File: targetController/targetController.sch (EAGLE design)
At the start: 52 parts, among them Q1 MOSFET-NCHANNELBSS123LT1G, Q10 2n3904, Q11 MOSFET-NCHANNELBSS123LT1G, Q12 2n3904, Q13 MOSFET-NCHANNELBSS123LT1G, Q14 2n3904, Q15 MOSFET-NCHANNELBSS123LT1G, Q16 2n3904, Q17 MOSFET-NCHANNELBSS123LT1G, Q18 2n3904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

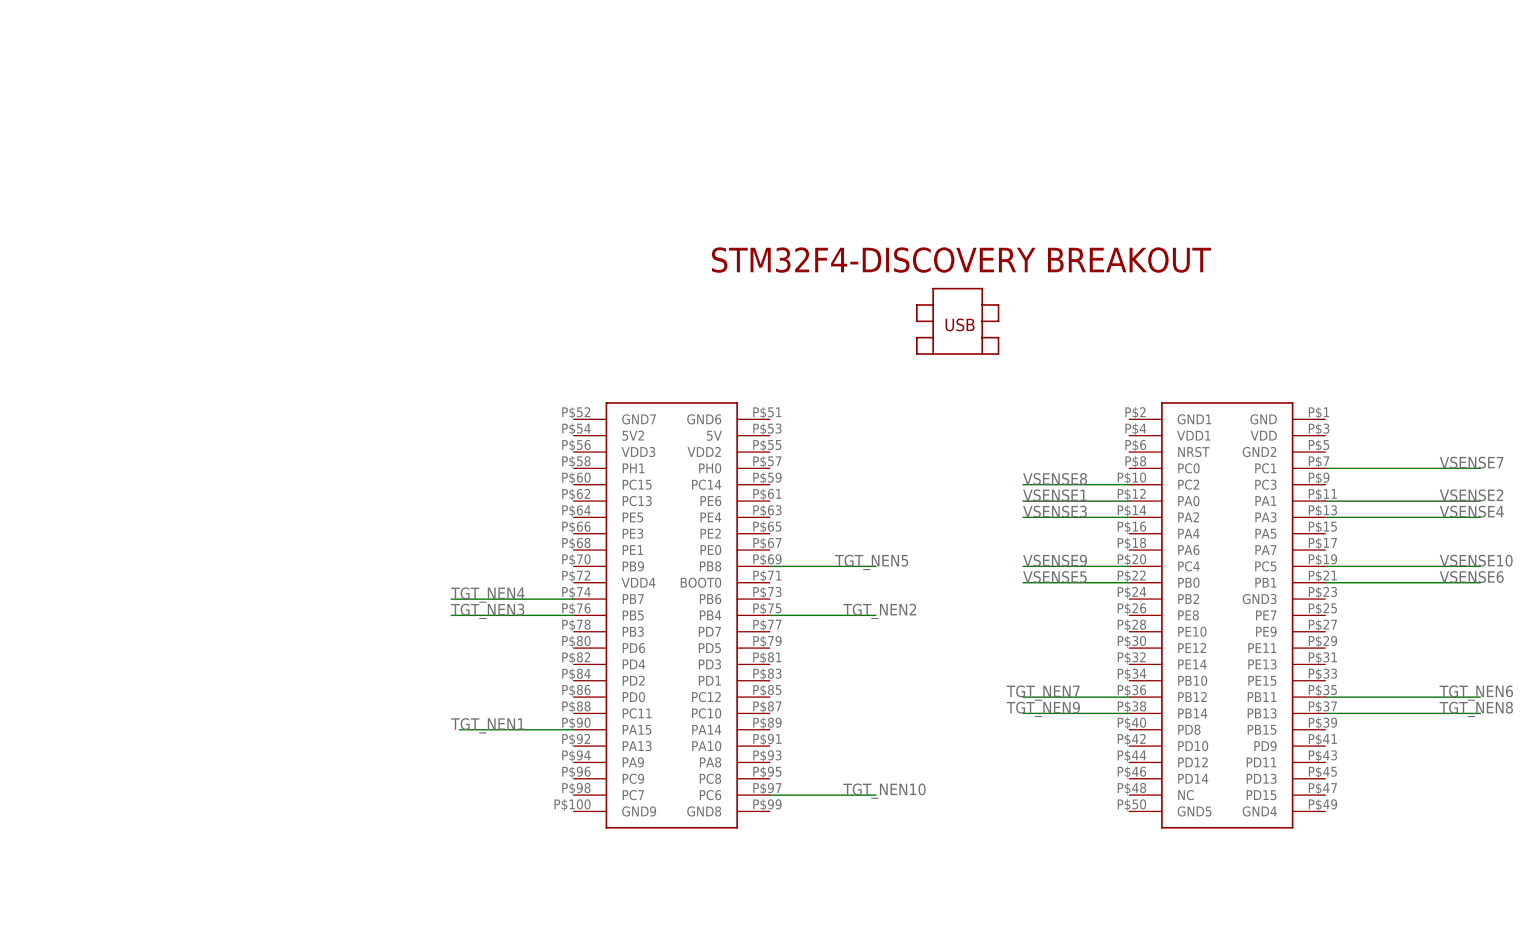
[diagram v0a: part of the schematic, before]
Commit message: Routed targetController
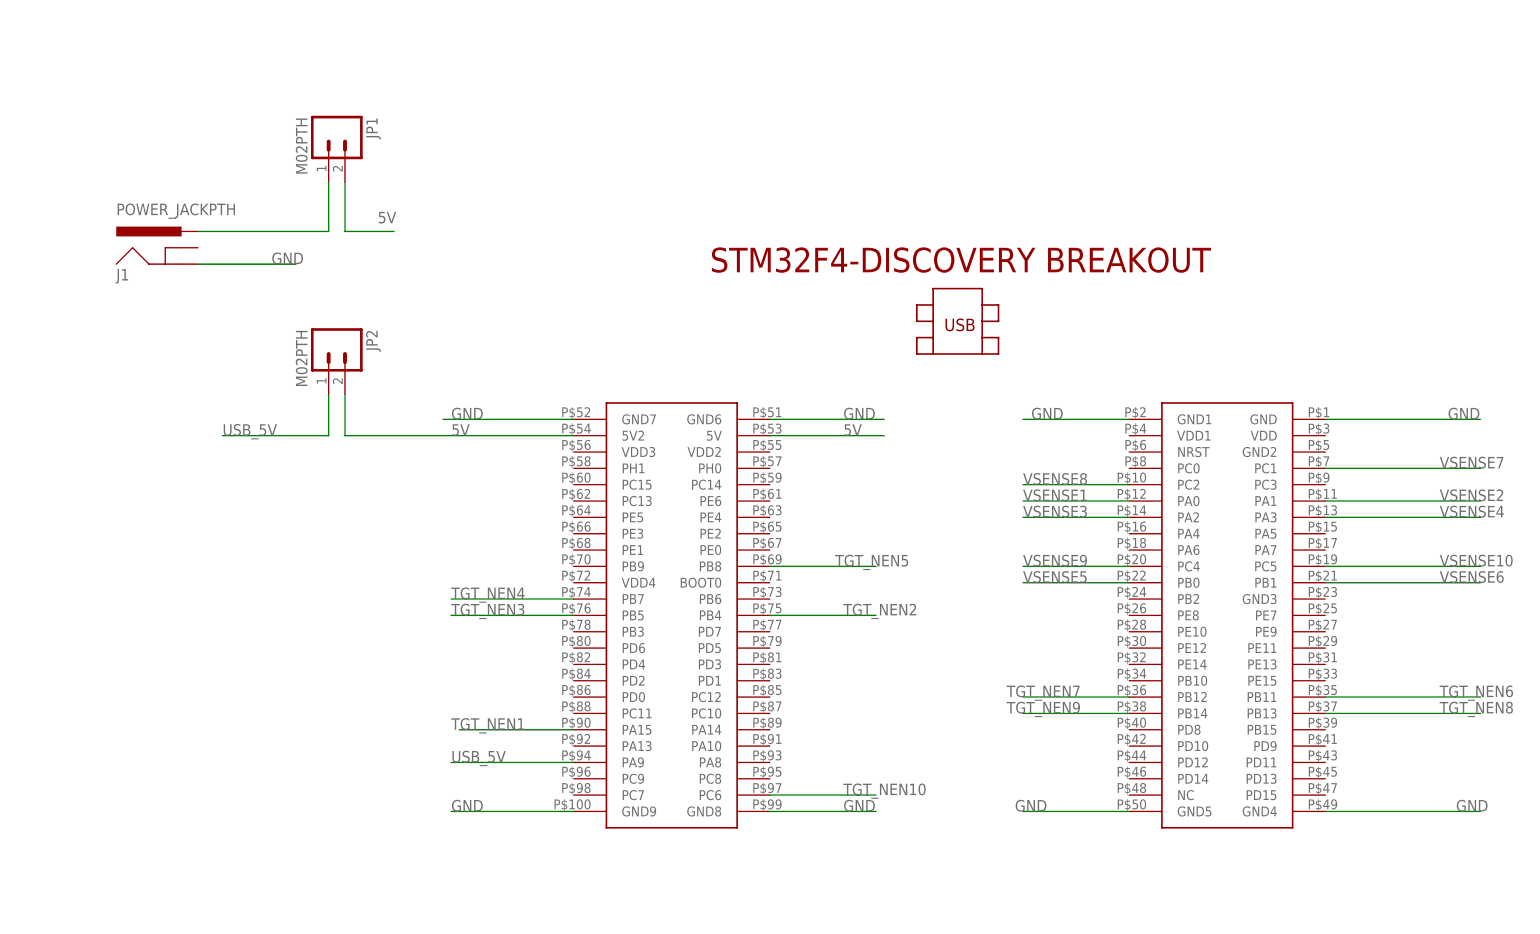
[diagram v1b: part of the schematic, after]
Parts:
- added J1: POWER_JACKPTH, SparkFun-Connectors:POWER_JACKPTH
- added JP1, JP2: M02PTH, SparkFun-Connectors:M02PTH
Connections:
- new net N$2: J1.PWR, JP1.1
- new net USB_5V: JP2.1, U$1.PA9
- net 5V: now also JP1.2, JP2.2, U$1.5V, U$1.5V2
- net GND: now also J1.GND, U$1.GND, U$1.GND1, U$1.GND4, U$1.GND5, U$1.GND6, U$1.GND7, U$1.GND8, U$1.GND9
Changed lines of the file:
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@@
 <setting verticaltext="up"/>
 </settings>
-<grid distance="0.1" unitdist="inch" unit="inch" style="lines" multiple="1" display="no" altdistance="0.01" altunitdist="inch" altunit="inch"/>
+<grid distance="0.05" unitdist="inch" unit="inch" style="lines" multiple="1" display="no" altdistance="0.025" altunitdist="inch" altunit="inch"/>
 <layers>
 <layer number="1" name="Top" color="4" fill="1" visible="no" active="no"/>
@@
 <part name="GND19" library="SparkFun-Aesthetics" deviceset="GND" device=""/>
 <part name="GND20" library="SparkFun-Aesthetics" deviceset="GND" device=""/>
+<part name="J1" library="SparkFun-Connectors" deviceset="POWER_JACK" device="PTH"/>
+<part name="JP1" library="SparkFun-Connectors" deviceset="M02" device="PTH"/>
+<part name="JP2" library="SparkFun-Connectors" deviceset="M02" device="PTH"/>
 </parts>
 <sheets>
@@
 <instance part="GND19" gate="1" x="-55.88" y="-287.02"/>
 <instance part="GND20" gate="1" x="-45.72" y="-287.02"/>
+<instance part="J1" gate="G$1" x="160.02" y="-68.58"/>
+<instance part="JP1" gate="G$1" x="182.88" y="-45.72" rot="R270"/>
+<instance part="JP2" gate="G$1" x="182.88" y="-78.74" rot="R270"/>
 </instances>
 <busses>
@@
 <wire x1="-45.72" y1="-284.48" x2="-45.72" y2="-274.32" width="0.1524" layer="91"/>
 </segment>
+<segment>
+<pinref part="U$1" gate="G$1" pin="GND7"/>
+<wire x1="220.98" y1="-90.17" x2="200.66" y2="-90.17" width="0.1524" layer="91"/>
+<label x="201.93" y="-90.17" size="1.778" layer="95"/>
+</segment>
+<segment>
+<pinref part="U$1" gate="G$1" pin="GND6"/>
+<wire x1="251.46" y1="-90.17" x2="269.24" y2="-90.17" width="0.1524" layer="91"/>
+<label x="262.89" y="-90.17" size="1.778" layer="95"/>
+</segment>
+<segment>
+<pinref part="J1" gate="G$1" pin="GND"/>
+<wire x1="162.56" y1="-66.04" x2="177.8" y2="-66.04" width="0.1524" layer="91"/>
+<label x="173.99" y="-66.04" size="1.778" layer="95"/>
+</segment>
+<segment>
+<pinref part="U$1" gate="G$1" pin="GND5"/>
+<wire x1="307.34" y1="-151.13" x2="290.83" y2="-151.13" width="0.1524" layer="91"/>
+<label x="289.56" y="-151.13" size="1.778" layer="95"/>
+</segment>
+<segment>
+<pinref part="U$1" gate="G$1" pin="GND4"/>
+<wire x1="337.82" y1="-151.13" x2="361.95" y2="-151.13" width="0.1524" layer="91"/>
+<label x="358.14" y="-151.13" size="1.778" layer="95"/>
+</segment>
+<segment>
+<pinref part="U$1" gate="G$1" pin="GND1"/>
+<wire x1="307.34" y1="-90.17" x2="290.83" y2="-90.17" width="0.1524" layer="91"/>
+<label x="292.1" y="-90.17" size="1.778" layer="95"/>
+</segment>
+<segment>
+<pinref part="U$1" gate="G$1" pin="GND"/>
+<wire x1="337.82" y1="-90.17" x2="361.95" y2="-90.17" width="0.1524" layer="91"/>
+<label x="356.87" y="-90.17" size="1.778" layer="95"/>
+</segment>
+<segment>
+<pinref part="U$1" gate="G$1" pin="GND8"/>
+<wire x1="251.46" y1="-151.13" x2="267.97" y2="-151.13" width="0.1524" layer="91"/>
+<label x="262.89" y="-151.13" size="1.778" layer="95"/>
+</segment>
+<segment>
+<pinref part="U$1" gate="G$1" pin="GND9"/>
+<wire x1="220.98" y1="-151.13" x2="201.93" y2="-151.13" width="0.1524" layer="91"/>
+<label x="201.93" y="-151.13" size="1.778" layer="95"/>
+</segment>
 </net>
 <net name="5V" class="0">
@@
 <pinref part="SUPPLY20" gate="G$1" pin="5V"/>
 <wire x1="-55.88" y1="-254" x2="-55.88" y2="-256.54" width="0.1524" layer="91"/>
+</segment>
+<segment>
+<pinref part="U$1" gate="G$1" pin="5V2"/>
+<wire x1="220.98" y1="-92.71" x2="185.42" y2="-92.71" width="0.1524" layer="91"/>
+<label x="201.93" y="-92.71" size="1.778" layer="95"/>
+<pinref part="JP2" gate="G$1" pin="2"/>
+<wire x1="185.42" y1="-92.71" x2="185.42" y2="-86.36" width="0.1524" layer="91"/>
+</segment>
+<segment>
+<pinref part="U$1" gate="G$1" pin="5V"/>
+<wire x1="251.46" y1="-92.71" x2="269.24" y2="-92.71" width="0.1524" layer="91"/>
+<label x="262.89" y="-92.71" size="1.778" layer="95"/>
+</segment>
+<segment>
+<pinref part="JP1" gate="G$1" pin="2"/>
+<wire x1="185.42" y1="-53.34" x2="185.42" y2="-60.96" width="0.1524" layer="91"/>
+<wire x1="185.42" y1="-60.96" x2="193.04" y2="-60.96" width="0.1524" layer="91"/>
+<label x="190.5" y="-59.69" size="1.778" layer="95"/>
 </segment>
 </net>
@@
 </segment>
 </net>
+<net name="N$2" class="0">
+<segment>
+<pinref part="J1" gate="G$1" pin="PWR"/>
+<wire x1="162.56" y1="-60.96" x2="182.88" y2="-60.96" width="0.1524" layer="91"/>
+<pinref part="JP1" gate="G$1" pin="1"/>
+<wire x1="182.88" y1="-60.96" x2="182.88" y2="-53.34" width="0.1524" layer="91"/>
+</segment>
+</net>
+<net name="USB_5V" class="0">
+<segment>
+<pinref part="U$1" gate="G$1" pin="PA9"/>
+<wire x1="220.98" y1="-143.51" x2="201.93" y2="-143.51" width="0.1524" layer="91"/>
+<label x="201.93" y="-143.51" size="1.778" layer="95"/>
+</segment>
+<segment>
+<pinref part="JP2" gate="G$1" pin="1"/>
+<wire x1="182.88" y1="-86.36" x2="182.88" y2="-92.71" width="0.1524" layer="91"/>
+<wire x1="182.88" y1="-92.71" x2="166.37" y2="-92.71" width="0.1524" layer="91"/>
+<label x="166.37" y="-92.71" size="1.778" layer="95"/>
+</segment>
+</net>
